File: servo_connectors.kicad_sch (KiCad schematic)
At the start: 15 parts, among them J10 Conn_01x03_Female, J11 Conn_01x03_Female, J12 Conn_01x03_Female, J13 Conn_01x03_Female, J14 Conn_01x03_Female, J15 Conn_01x04_MountingPin, J16 Conn_01x04_MountingPin, J17 Conn_01x04_MountingPin, J3 Conn_01x03_Female, J4 Conn_01x03_Female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

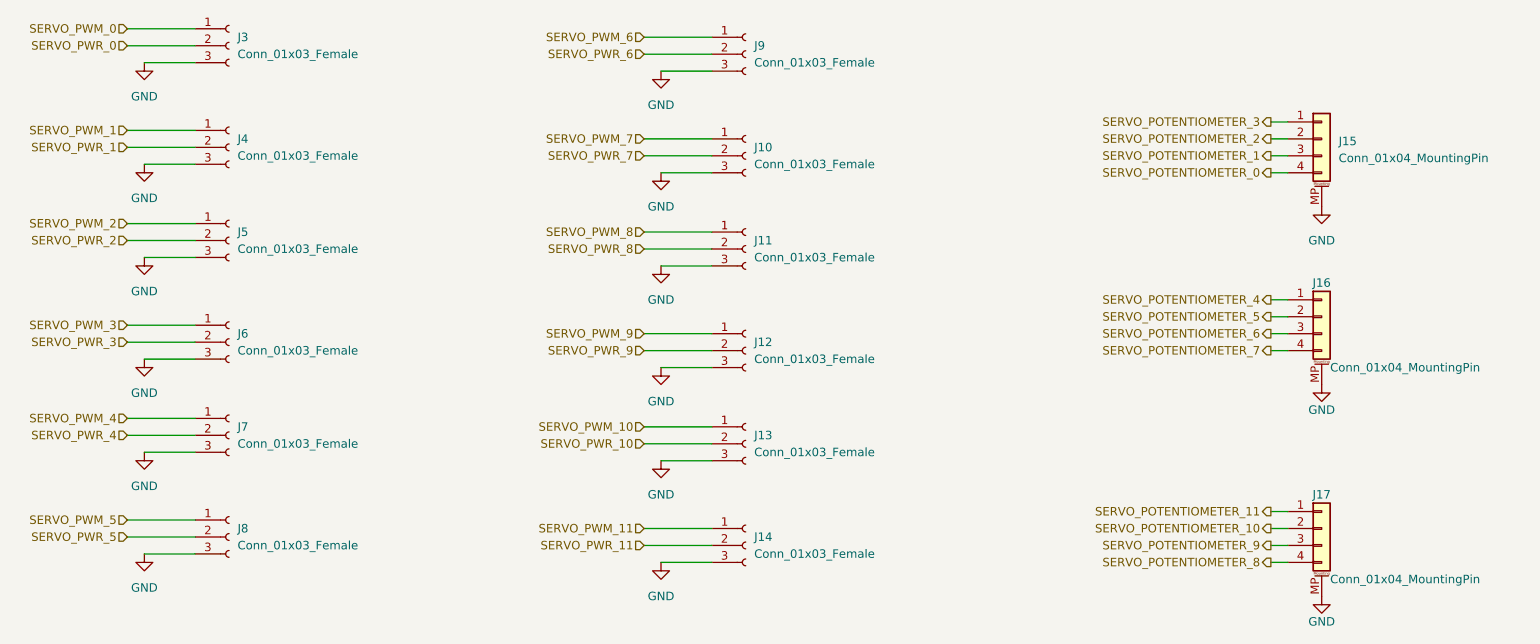
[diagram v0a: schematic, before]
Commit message: Bord v1.2, added flash memory, changed pinout od servomotor connectors and removed potentiometer signal from servomotors plus one ADC
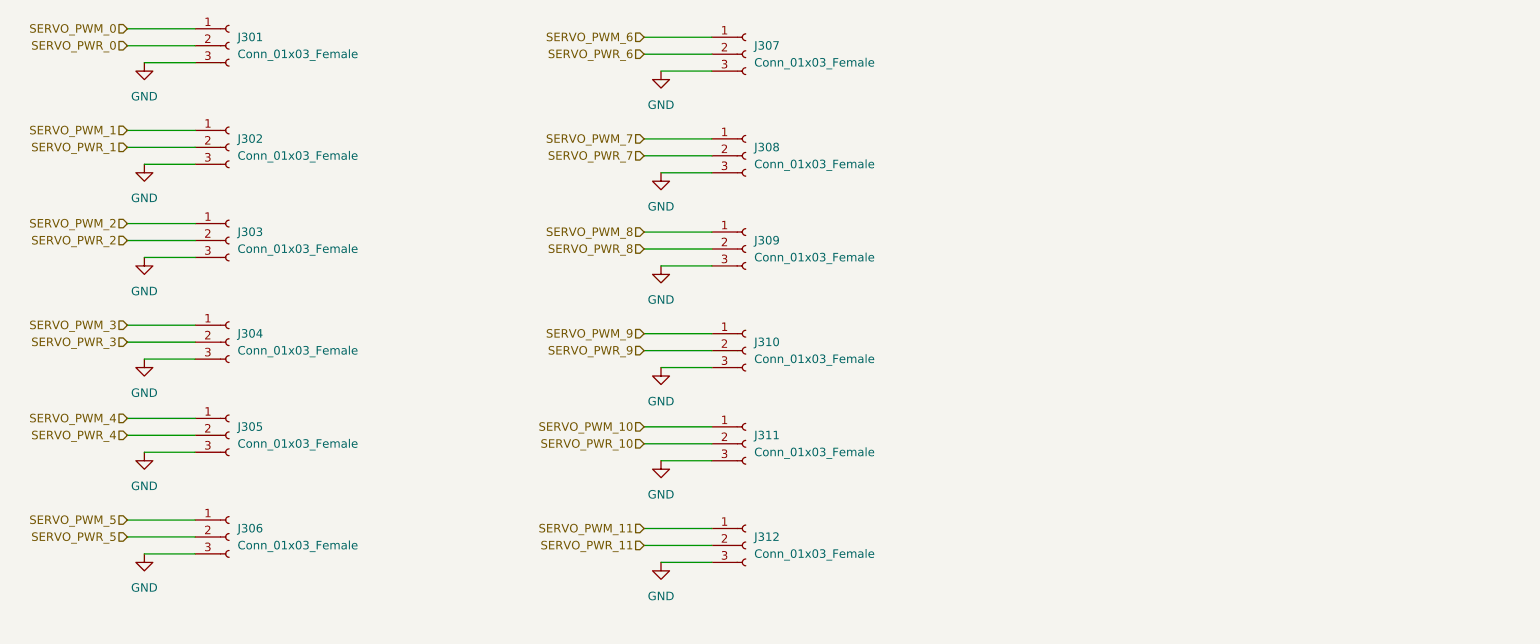
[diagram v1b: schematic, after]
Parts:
- removed J15, J16, J17: Conn_01x04_MountingPin, Connector_Molex:Molex_CLIK-Mate_502382-0470_1x04-1MP_P1.25mm_Vertical, symbol Connector_Generic_MountingPin:Conn_01x04_MountingPin
- J301: renamed from J3; footprint Connector_PinHeader_1.27mm:PinHeader_1x03_P1.27mm_Vertical -> Connector_PinHeader_2.54mm:PinHeader_1x03_P2.54mm_Vertical
- J302: renamed from J4; footprint Connector_PinHeader_1.27mm:PinHeader_1x03_P1.27mm_Vertical -> Connector_PinHeader_2.54mm:PinHeader_1x03_P2.54mm_Vertical
- J303: renamed from J5; footprint Connector_PinHeader_1.27mm:PinHeader_1x03_P1.27mm_Vertical -> Connector_PinHeader_2.54mm:PinHeader_1x03_P2.54mm_Vertical
- J304: renamed from J6; footprint Connector_PinHeader_1.27mm:PinHeader_1x03_P1.27mm_Vertical -> Connector_PinHeader_2.54mm:PinHeader_1x03_P2.54mm_Vertical
- J305: renamed from J7; footprint Connector_PinHeader_1.27mm:PinHeader_1x03_P1.27mm_Vertical -> Connector_PinHeader_2.54mm:PinHeader_1x03_P2.54mm_Vertical
- J306: renamed from J8; footprint Connector_PinHeader_1.27mm:PinHeader_1x03_P1.27mm_Vertical -> Connector_PinHeader_2.54mm:PinHeader_1x03_P2.54mm_Vertical
- J307: renamed from J9; footprint Connector_PinHeader_1.27mm:PinHeader_1x03_P1.27mm_Vertical -> Connector_PinHeader_2.54mm:PinHeader_1x03_P2.54mm_Vertical
- J308: renamed from J10; footprint Connector_PinHeader_1.27mm:PinHeader_1x03_P1.27mm_Vertical -> Connector_PinHeader_2.54mm:PinHeader_1x03_P2.54mm_Vertical
- J309: renamed from J11; footprint Connector_PinHeader_1.27mm:PinHeader_1x03_P1.27mm_Vertical -> Connector_PinHeader_2.54mm:PinHeader_1x03_P2.54mm_Vertical
- J310: renamed from J12; footprint Connector_PinHeader_1.27mm:PinHeader_1x03_P1.27mm_Vertical -> Connector_PinHeader_2.54mm:PinHeader_1x03_P2.54mm_Vertical
- J311: renamed from J13; footprint Connector_PinHeader_1.27mm:PinHeader_1x03_P1.27mm_Vertical -> Connector_PinHeader_2.54mm:PinHeader_1x03_P2.54mm_Vertical
- J312: renamed from J14; footprint Connector_PinHeader_1.27mm:PinHeader_1x03_P1.27mm_Vertical -> Connector_PinHeader_2.54mm:PinHeader_1x03_P2.54mm_Vertical
